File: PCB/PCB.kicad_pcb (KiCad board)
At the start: 2 copper layers, 119.9 x 90.3 mm, 42 parts, among them IC2 AP33771CFBZ-13-FA01, IC3 LT8609EMSE#PBF, IC4 AP63203WU-7, J3 UJ20-C-V-SMT-TR-68, J6 USBC_Power_Breakout, Q1 PSMN2R6-30YLC,115, Q2 PSMN2R6-30YLC,115

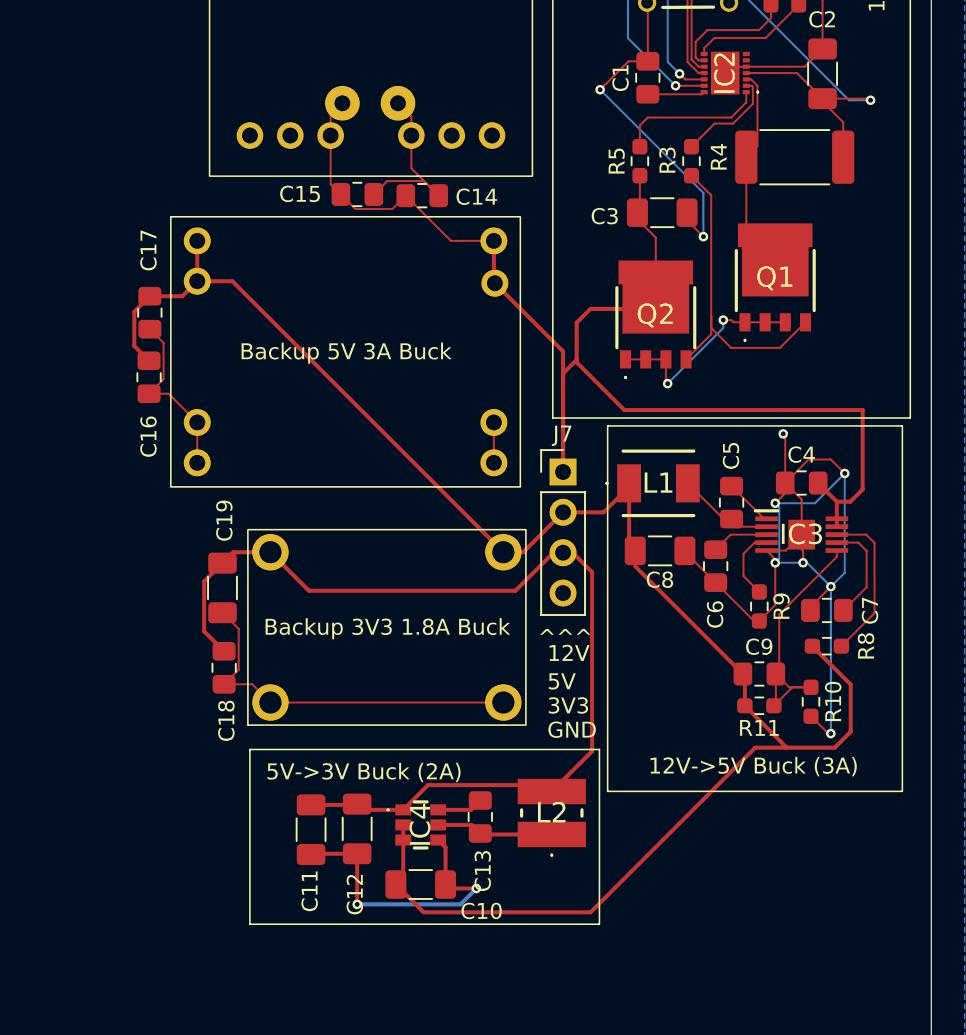
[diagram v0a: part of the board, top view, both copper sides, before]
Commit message: schematic update
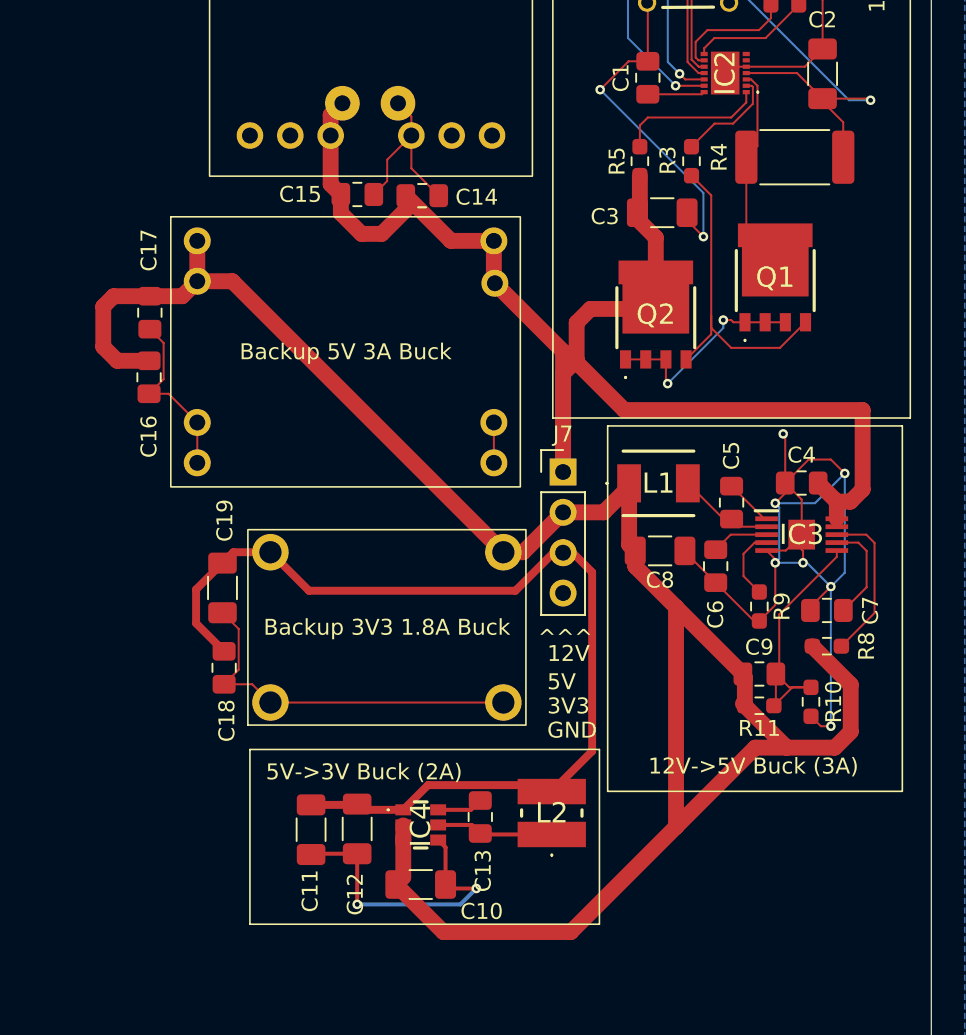
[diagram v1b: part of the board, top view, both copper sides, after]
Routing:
- net +5V: track 112.3 -> 131.2 mm
- net +12V: track 84.3 -> 86.3 mm
- net GND: track 217.6 -> 216.8 mm

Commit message: complete pcb
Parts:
- added C20: 0.1uF, Capacitor_SMD:C_0805_2012Metric_Pad1.18x1.45mm_HandSolder, F.Cu at (32.8, 102.8)
- added C21: 4.7uF, Capacitor_SMD:C_0805_2012Metric_Pad1.18x1.45mm_HandSolder, F.Cu at (27.8, 102.8)
- added C22: 4.7uF, Capacitor_SMD:C_0805_2012Metric_Pad1.18x1.45mm_HandSolder, F.Cu at (88.1, 82.0)
- added C23: 0.1uF, Capacitor_SMD:C_0805_2012Metric_Pad1.18x1.45mm_HandSolder, F.Cu at (88.1, 86.7)
- added C24: 47uF, Capacitor_SMD:C_0805_2012Metric_Pad1.18x1.45mm_HandSolder, F.Cu at (81.8, 24.8)
- added C25: 0.1uF, Capacitor_SMD:C_0805_2012Metric_Pad1.18x1.45mm_HandSolder, F.Cu at (81.8, 27.8)
- added C26: 0.1uF, Capacitor_SMD:C_0805_2012Metric_Pad1.18x1.45mm_HandSolder, F.Cu at (58.2, 25.7)
- added C27: 22uF, Capacitor_SMD:C_1206_3216Metric_Pad1.33x1.80mm_HandSolder, F.Cu at (50.2, 26.5)
- added C28: 0.1uF, Capacitor_SMD:C_0805_2012Metric_Pad1.18x1.45mm_HandSolder, F.Cu at (47.0, 26.5)
- added C29: 10uF, Capacitor_SMD:C_1206_3216Metric_Pad1.33x1.80mm_HandSolder, F.Cu at (41.4, 33.5)
- added C30: 0.1uF, Capacitor_SMD:C_0805_2012Metric_Pad1.18x1.45mm_HandSolder, F.Cu at (37.6, 33.4)
- added C31: 4.7uF, Capacitor_SMD:C_0805_2012Metric_Pad1.18x1.45mm_HandSolder, F.Cu at (109.7, 88.3)
- added C32: 0.1uF, Capacitor_SMD:C_0805_2012Metric_Pad1.18x1.45mm_HandSolder, F.Cu at (109.7, 91.3)
- added C33: 22uF, Capacitor_SMD:C_1206_3216Metric_Pad1.33x1.80mm_HandSolder, F.Cu at (79.4, 33.4)
- added C34: 0.1uF, Capacitor_SMD:C_0805_2012Metric_Pad1.18x1.45mm_HandSolder, F.Cu at (79.2, 38.9)
- added IC1: MSPM0G3507SDGS28R, SpinnyKitty:SOP50P490X110-28N, F.Cu at (57.8, 31.2)
- added J1: ICS43434 Breakout, SpinnyKitty:ICS43434 Breakout, F.Cu at (99.0, 98.0)
- added J2: MAX98357_Breakout, SpinnyKitty:MAX98357, F.Cu at (24.6, 19.0)
- added J4: LED_Header, Connector_PinHeader_2.54mm:PinHeader_1x03_P2.54mm_Vertical, F.Cu at (50.3, 21.6)
- added J5: MSPM0 Programming Header, Connector_PinHeader_2.54mm:PinHeader_1x05_P2.54mm_Vertical, F.Cu at (42.5, 17.0)
- added J8: Motor_Driver_Power, Connector_PinHeader_2.54mm:PinHeader_1x02_P2.54mm_Vertical, F.Cu at (82.9, 21.8)
- added J9: ~, Connector_PinHeader_2.54mm:PinHeader_1x04_P2.54mm_Vertical, F.Cu at (66.3, 17.8)
- added R12: 2.2k, Resistor_SMD:R_0603_1608Metric_Pad0.98x0.95mm_HandSolder, F.Cu at (63.9, 67.0)
- added R13: 2.2k, Resistor_SMD:R_0603_1608Metric_Pad0.98x0.95mm_HandSolder, F.Cu at (64.0, 64.0)
- added R14: 10k, Resistor_SMD:R_0603_1608Metric_Pad0.98x0.95mm_HandSolder, F.Cu at (18.0, 102.0)
- added R15: 10k, Resistor_SMD:R_0603_1608Metric_Pad0.98x0.95mm_HandSolder, F.Cu at (18.0, 94.0)
- added R16: 10k, Resistor_SMD:R_0603_1608Metric_Pad0.98x0.95mm_HandSolder, F.Cu at (18.0, 78.0)
- added R17: 10k, Resistor_SMD:R_0603_1608Metric_Pad0.98x0.95mm_HandSolder, F.Cu at (18.0, 86.0)
- added R18: 10k, Resistor_SMD:R_0603_1608Metric_Pad0.98x0.95mm_HandSolder, F.Cu at (18.0, 62.0)
- added R19: 10k, Resistor_SMD:R_0603_1608Metric_Pad0.98x0.95mm_HandSolder, F.Cu at (18.0, 70.0)
- added R20: 10k, Resistor_SMD:R_0603_1608Metric_Pad0.98x0.95mm_HandSolder, F.Cu at (18.0, 54.0)
- added R21: 10k, Resistor_SMD:R_0603_1608Metric_Pad0.98x0.95mm_HandSolder, F.Cu at (18.0, 46.0)
- added S1: TL3305AF260QG, SpinnyKitty:TL3305AF160QG, F.Cu at (23.0, 98.0)
- added S2: TL3305AF260QG, SpinnyKitty:TL3305AF160QG, F.Cu at (23.0, 90.0)
- added S3: TL3305AF260QG, SpinnyKitty:TL3305AF160QG, F.Cu at (23.0, 74.0)
- added S4: TL3305AF260QG, SpinnyKitty:TL3305AF160QG, F.Cu at (23.0, 82.0)
- added S5: TL3305AF260QG, SpinnyKitty:TL3305AF160QG, F.Cu at (23.0, 58.0)
- added S6: TL3305AF260QG, SpinnyKitty:TL3305AF160QG, F.Cu at (23.0, 66.0)
- added S7: TL3305AF260QG, SpinnyKitty:TL3305AF160QG, F.Cu at (23.0, 50.0)
- added S8: TL3305AF260QG, SpinnyKitty:TL3305AF160QG, F.Cu at (23.0, 42.0)
- added U1: ~, SpinnyKitty:ESP32_30pin, F.Cu at (44.0, 76.0)
- added U2: 254, SpinnyKitty:MODULE_254, F.Cu at (74.0, 86.0)
- added U5: SN74AHCT125N, SpinnyKitty:DIP794W45P254L1930H508Q14, F.Cu at (70.5, 36.3)
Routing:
- net +3V3: track 64.5 -> 433.7 mm
- net +5V: track 131.2 -> 425.9 mm, vias 0 -> 4
- net GND: track 216.8 -> 508.5 mm, vias 11 -> 16
- net /SCL: track 0.00 -> 102.5 mm, vias 0 -> 1
- net /SDA: track 0.00 -> 100.0 mm, vias 0 -> 2
- net /MIC_DOUT: track 0.00 -> 91.2 mm, vias 0 -> 1
- net /MIC_BCLK: track 0.00 -> 85.9 mm, vias 0 -> 1
- net /AMP_DIN: track 0.00 -> 67.2 mm
- net /AMP_BCLK: track 0.00 -> 63.2 mm
- net /AMP_LRC: track 0.00 -> 58.2 mm
- net /MTX_ERX: track 0.00 -> 54.3 mm, vias 0 -> 1
- net /ETX_MRX: track 0.00 -> 50.6 mm, vias 0 -> 1
- net /MIC_LRCL: track 0.00 -> 40.8 mm, vias 0 -> 1
- net /BTN_MTR: track 0.00 -> 39.4 mm, vias 0 -> 2
- net /BTN_LED: track 0.00 -> 35.3 mm, vias 0 -> 2
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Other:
- board size 119.9 x 90.3 mm -> 120 x 97 mm
- board text added: "+"
- board text added: "-"
- board text added: "D"
- board text added: "ENA"
- board text added: "IN1"
- board text added: "IN2"
- board text added: "LED"
- board text added: "LGC SHFT"
- board text added: "MD CTRL"
- board text added: "MD PWR"
- board text added: "MSPM0"
- board text added: "MTR"
- board text added: "NRST"
- board text added: "NXT"
- board text added: "OIIA"
- board text added: "PRV"
- board text added: "SPK"
- board text added: "SWCLK"
- board text added: "SWDIO"
- board text added: "Spinny Kitty Committee V1 Katherine Han Evan Ho Hajime Kioi Winson Lin"
- board text added: "VOL+"
- board text added: "VOL-"
- board text added: "▷ II"

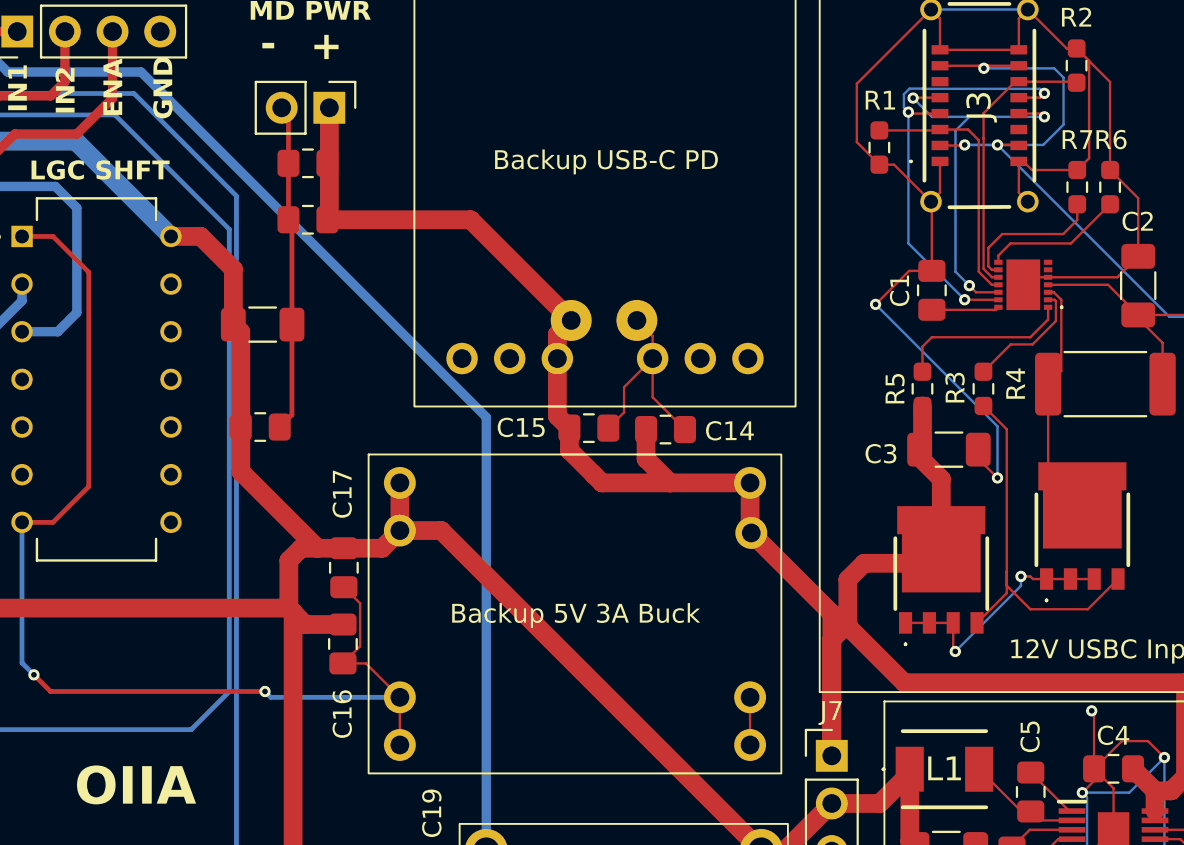
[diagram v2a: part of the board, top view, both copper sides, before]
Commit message: routing cleanup
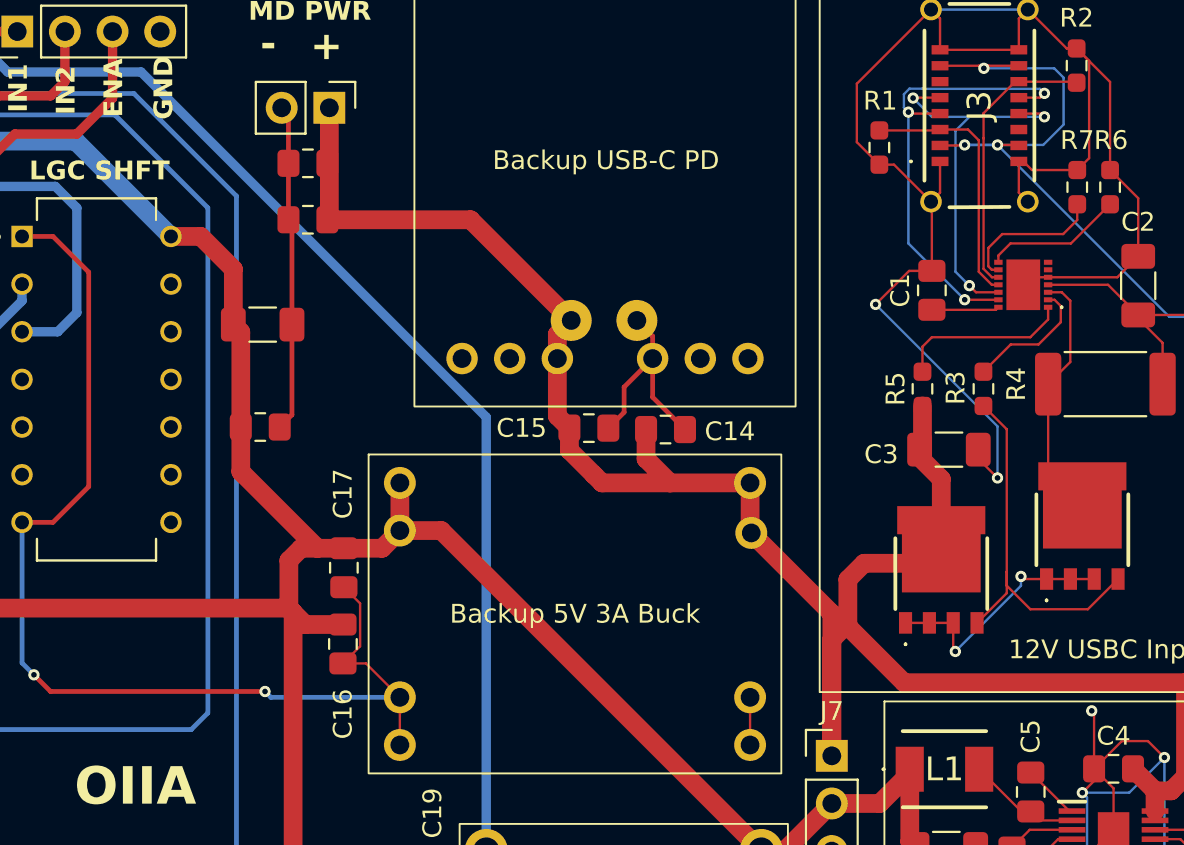
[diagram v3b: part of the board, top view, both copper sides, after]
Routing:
- net /SCL: track 102.5 -> 101.5 mm
- net /VBUS_SW_IN: track 13.6 -> 14.3 mm
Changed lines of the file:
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@@
 	)
 	(segment
-		(start 121.548624 31.6784)
-		(end 121.947999 32.077775)
+		(start 122.428 35.3952)
+		(end 121.248 36.5752)
 		(width 0.127)
 		(layer "F.Cu")
@@
 	(segment
 		(start 121.245 31.6784)
-		(end 121.548624 31.6784)
+		(end 121.9754 31.6784)
 		(width 0.127)
 		(layer "F.Cu")
@@
 	)
 	(segment
-		(start 121.947999 35.875201)
-		(end 121.248 36.5752)
+		(start 121.9754 31.6784)
+		(end 122.428 32.131)
 		(width 0.127)
 		(layer "F.Cu")
@@
 	)
 	(segment
-		(start 121.947999 32.077775)
-		(end 121.947999 35.875201)
+		(start 122.428 32.131)
+		(end 122.428 35.3952)
 		(width 0.127)
 		(layer "F.Cu")
@@
 	)
 	(segment
-		(start 121.6615 32.1519)
-		(end 121.6615 33.2117)
+		(start 121.245 32.0784)
+		(end 121.588 32.0784)
 		(width 0.127)
 		(layer "F.Cu")
@@
 	)
 	(segment
-		(start 121.6615 33.2117)
-		(end 120.4145 34.4587)
+		(start 120.7353 34.4587)
+		(end 119.252 34.4587)
 		(width 0.127)
 		(layer "F.Cu")
@@
 	)
 	(segment
-		(start 121.588 32.0784)
-		(end 121.6615 32.1519)
+		(start 121.92 33.274)
+		(end 120.7353 34.4587)
 		(width 0.127)
 		(layer "F.Cu")
@@
 	)
 	(segment
-		(start 120.4145 34.4587)
-		(end 119.252 34.4587)
+		(start 121.92 32.4104)
+		(end 121.92 33.274)
 		(width 0.127)
 		(layer "F.Cu")
@@
 	)
 	(segment
-		(start 121.245 32.0784)
-		(end 121.588 32.0784)
+		(start 121.588 32.0784)
+		(end 121.92 32.4104)
 		(width 0.127)
 		(layer "F.Cu")
@@
 	)
 	(segment
-		(start 120.437 46.9642)
-		(end 121.1646 46.9642)
+		(start 119.798 46.8252)
+		(end 119.937 46.9642)
 		(width 0.127)
 		(layer "F.Cu")
@@
 	)
 	(segment
-		(start 120.298 46.8252)
-		(end 120.437 46.9642)
-		(width 0.127)
-		(layer "F.Cu")
-		(net 17)
-	)
-	(segment
 		(start 116.1862 50.7134)
 		(end 116.298 50.8252)
@@
 	)
 	(segment
-		(start 113.6462 49.301)
-		(end 116.1862 49.301)
+		(start 119.937 46.9642)
+		(end 121.1646 46.9642)
 		(width 0.127)
 		(layer "F.Cu")
@@
 	)
 	(segment
-		(start 119.798 46.8252)
-		(end 120.298 46.8252)
+		(start 113.6462 49.301)
+		(end 116.1862 49.301)
 		(width 0.127)
 		(layer "F.Cu")
@@
 	)
 	(segment
-		(start 77.597 52.959)
-		(end 77.597 28.321)
+		(start 76.454 54.102)
+		(end 76.454 27.178)
 		(width 0.254)
 		(layer "B.Cu")
@@
 	)
 	(segment
-		(start 75.565 54.991)
-		(end 77.597 52.959)
+		(start 55.173813 59.999813)
+		(end 54.425823 59.251823)
 		(width 0.254)
 		(layer "B.Cu")
@@
 	)
 	(segment
-		(start 55.173813 59.999813)
-		(end 54.425823 59.251823)
+		(start 76.454 27.178)
+		(end 71.501 22.225)
 		(width 0.254)
 		(layer "B.Cu")
@@
 	)
 	(segment
-		(start 54.425823 56.953176)
-		(end 56.388 54.991)
+		(start 57.47246 59.999813)
+		(end 55.173813 59.999813)
 		(width 0.254)
 		(layer "B.Cu")
@@
 	)
 	(segment
-		(start 71.501 22.225)
-		(end 64.516 22.225)
+		(start 75.565 54.991)
+		(end 76.454 54.102)
 		(width 0.254)
 		(layer "B.Cu")
@@
 	)
 	(segment
-		(start 77.597 28.321)
-		(end 71.501 22.225)
+		(start 56.388 54.991)
+		(end 75.565 54.991)
 		(width 0.254)
 		(layer "B.Cu")
@@
 	)
 	(segment
-		(start 54.425823 59.251823)
-		(end 54.425823 56.953176)
+		(start 54.425823 56.953176)
+		(end 56.388 54.991)
 		(width 0.254)
 		(layer "B.Cu")
@@
 	)
 	(segment
-		(start 56.388 54.991)
-		(end 75.565 54.991)
+		(start 71.501 22.225)
+		(end 64.516 22.225)
 		(width 0.254)
 		(layer "B.Cu")
@@
 	)
 	(segment
-		(start 64.516 22.225)
-		(end 58.039 15.748)
+		(start 54.425823 59.251823)
+		(end 54.425823 56.953176)
 		(width 0.254)
 		(layer "B.Cu")
@@
 	)
 	(segment
-		(start 57.47246 59.999813)
-		(end 55.173813 59.999813)
+		(start 64.516 22.225)
+		(end 58.039 15.748)
 		(width 0.254)
 		(layer "B.Cu")
@@
 		(start 97.802 38.9194)
 		(end 98.6423 38.0791)
-		(width 0.127)
+		(width 0.254)
 		(layer "F.Cu")
 		(net 66)
@@
 		(start 98.6423 36.7329)
 		(end 100.1642 35.211)
-		(width 0.127)
+		(width 0.254)
 		(layer "F.Cu")
 		(net 66)
@@
 		(start 99.3242 33.179)
 		(end 100.1642 34.019)
-		(width 0.127)
+		(width 0.254)
 		(layer "F.Cu")
 		(net 66)
@@
 		(start 98.6423 38.0791)
 		(end 98.6423 36.7329)
-		(width 0.127)
+		(width 0.254)
 		(layer "F.Cu")
 		(net 66)
@@
 		(start 100.1642 34.019)
 		(end 100.1642 35.211)
-		(width 0.127)
+		(width 0.254)
 		(layer "F.Cu")
 		(net 66)
@@
 		(start 100.1642 35.211)
 		(end 100.1642 37.2723)
-		(width 0.127)
+		(width 0.254)
 		(layer "F.Cu")
 		(net 66)
@@
 		(start 100.1642 37.2723)
 		(end 101.8875 38.9956)
-		(width 0.127)
+		(width 0.254)
 		(layer "F.Cu")
 		(net 66)

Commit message: mspm0 update
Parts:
- added C35: 10uF, Capacitor_SMD:C_1206_3216Metric_Pad1.33x1.80mm_HandSolder, F.Cu at (53.1, 26.5)
- added C36: 10nF, Capacitor_SMD:C_0805_2012Metric_Pad1.18x1.45mm_HandSolder, F.Cu at (57.3, 23.7)
- added C37: 0.47uF, Capacitor_SMD:C_0805_2012Metric_Pad1.18x1.45mm_HandSolder, F.Cu at (61.6, 25.9)
- added R22: 47k, Resistor_SMD:R_0603_1608Metric_Pad0.98x0.95mm_HandSolder, F.Cu at (57.4, 25.7)
- moved R12 47.6 mm to (61.5, 19.5), turned to -90 degrees
- moved R13 44.9 mm to (58.0, 19.5), turned to -90 degrees
- moved C26 5.55 mm to (52.8, 24.1)
- moved J4 3.76 mm to (46.6, 20.8)
- moved C27 2.03 mm to (48.1, 26.5)
- moved C28 1.40 mm to (45.6, 26.5)
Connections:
- IC1 pad 3: unconnected-(IC1-VCORE-Pad3) -> /VCORE
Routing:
- net +3V3: track 433.7 -> 452.1 mm, vias 0 -> 2
- net GND: track 508.5 -> 520.6 mm, vias 16 -> 18
- net /SCL: track 101.5 -> 95.2 mm
- net +5V: track 425.9 -> 430.7 mm
- net /LED_SHIFTED: track 27.9 -> 31.9 mm
- net /NRST: track 20.1 -> 23.6 mm
- net /VCORE: track 0.00 -> 2.83 mm
- net /DP: track 25.0 -> 26.3 mm
- net /GATE_DRV: track 20.6 -> 21.9 mm
- net /AMP_LRC: track 58.2 -> 59.3 mm
- net Net-(IC2-VSEL): track 7.45 -> 8.19 mm
- net /BTN_PRV: track 14.2 -> 13.5 mm

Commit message: pcb backups
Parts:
- added R23: 100k, Resistor_SMD:R_0805_2012Metric_Pad1.20x1.40mm_HandSolder, F.Cu at (52.8, 30.2)
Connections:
- IC1 pad 9: unconnected-(IC1-PA2_/_ROSC-Pad9) -> Net-(IC1-PA2_/_ROSC)
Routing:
- net Net-(IC1-PA2_/_ROSC): track 0.00 -> 6.63 mm
- net GND: track 520.6 -> 522.0 mm, vias 18 -> 19
